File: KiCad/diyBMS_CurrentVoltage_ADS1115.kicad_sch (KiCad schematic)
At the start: 51 parts, among them J1 Conn_01x10_MountingPin, J3 Debug/UPDI, J3 PA3/PA4, J4 9x9 PIN connector, J5 9x9 PIN connector, J5 Screw_Terminal_01x04, J6 Screw_Terminal_01x02, J7 Screw_Terminal_01x02, U1 ACPL-C870, U2 ADS1115IDGS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

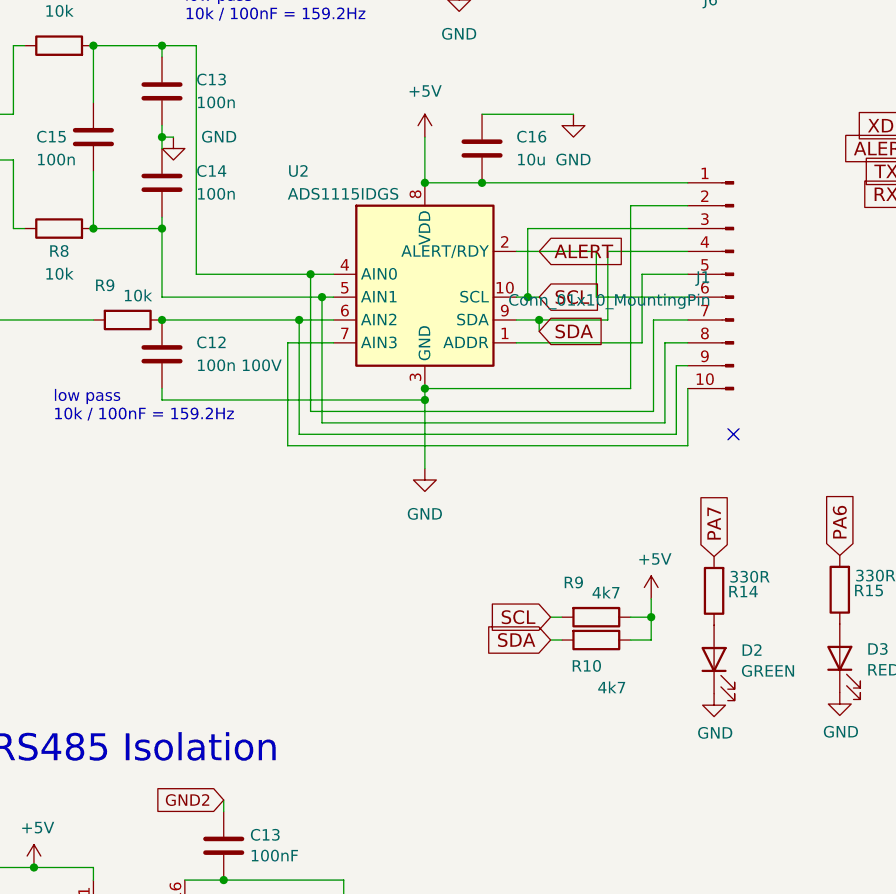
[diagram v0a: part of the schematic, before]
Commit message: working including MODBUS RTU
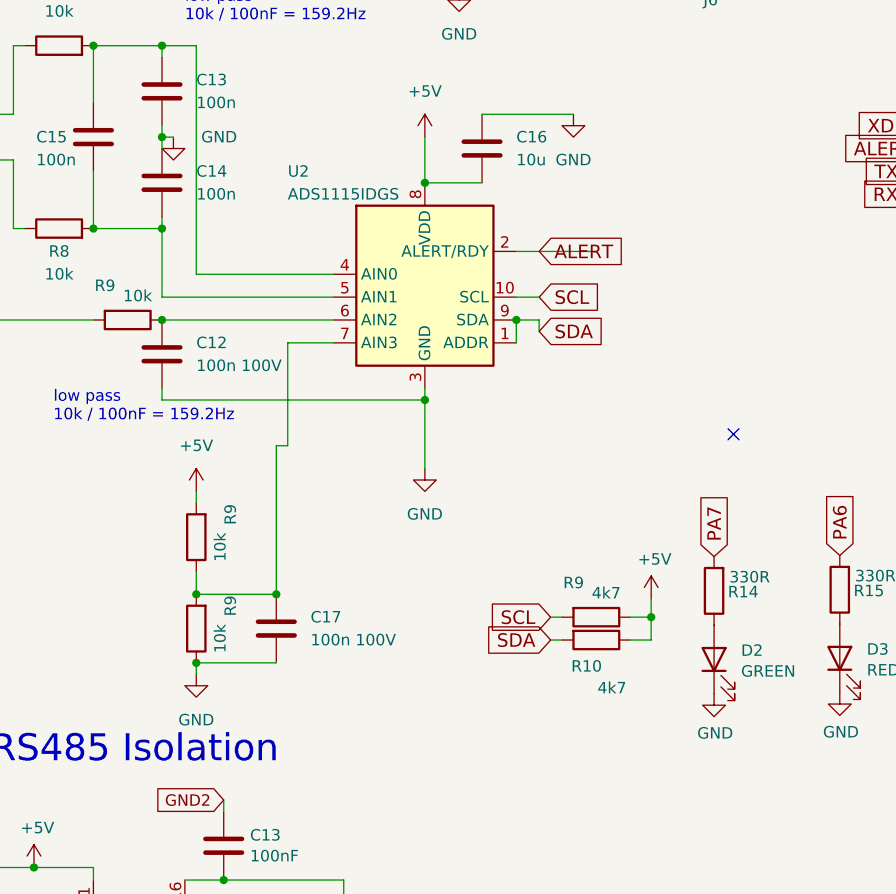
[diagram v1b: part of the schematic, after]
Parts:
- removed J1: Conn_01x10_MountingPin, Connector_PinHeader_2.54mm:PinHeader_1x10_P2.54mm_Vertical, symbol Connector:Conn_01x10_Pin
- added C17: 100n 100V, Capacitor_SMD:C_0805_2012Metric, symbol Device:C
- added R9 (x2): 10k, Resistor_SMD:R_0805_2012Metric, symbol Device:R
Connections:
- net +5V: now also R9.2
- net GND: now also C17.2, R9.1
- net SDA: now also U2.1 (ADDR)
- net at U2.7 (AIN3): now also C17.1, R9.1, R9.2
